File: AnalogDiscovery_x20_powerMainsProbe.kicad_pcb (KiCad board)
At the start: 2 copper layers, 64 x 64 mm, 32 parts, among them J1 Conn_02x15_Counter_Clockwise, J2 Conn_01x03_Female, J3 Conn_01x03_Female, J4 Conn_01x03_Male, J5 Conn_01x03_Male, J6 Conn_02x03_Counter_Clockwise

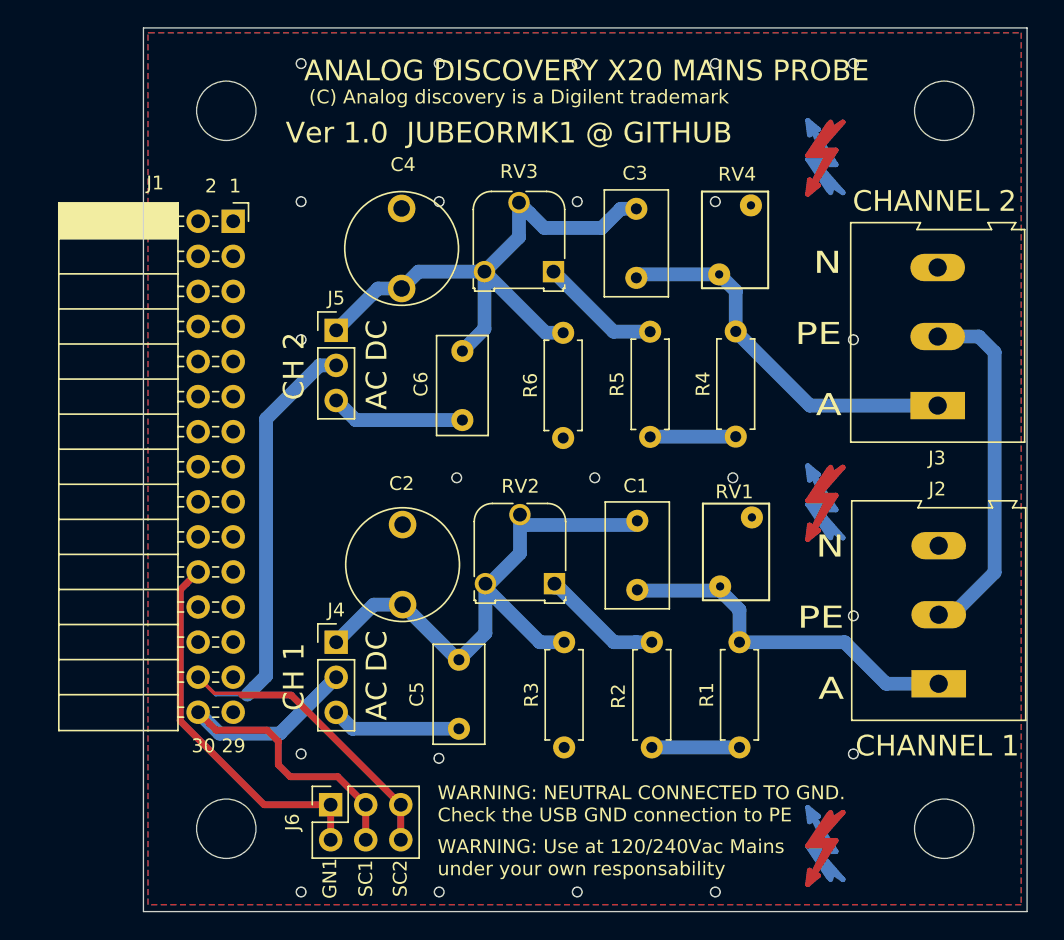
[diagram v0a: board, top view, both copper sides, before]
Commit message: Solved issue #10
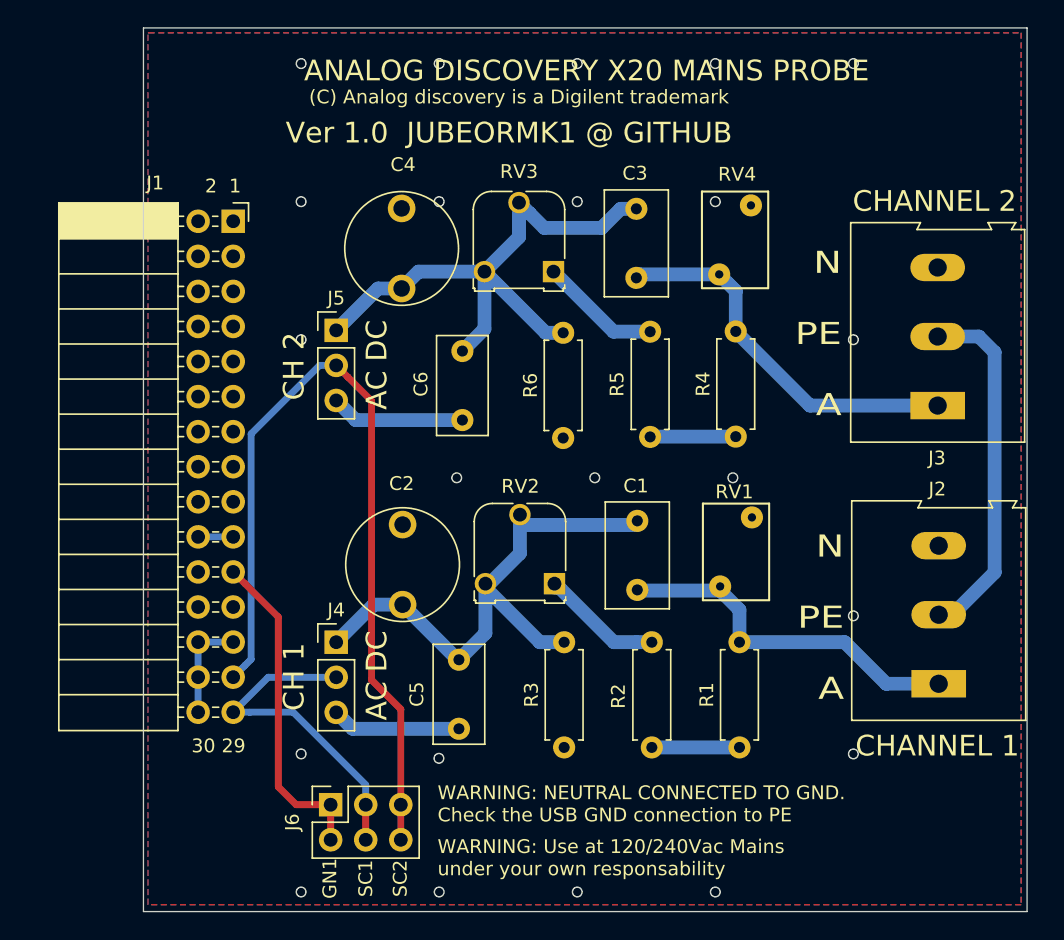
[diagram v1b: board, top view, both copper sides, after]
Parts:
- removed REF** (x6): Symbol_Highvoltage_Type1_CopperTop_Small, Symbol:Symbol_Highvoltage_Type1_CopperTop_Small
- removed REF** (x4): MountingHole_4.3mm_M4, MountingHole:MountingHole_4.3mm_M4
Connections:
- J1 pad 1: /DIO_15 -> (no net)
- J1 pad 10: /DIO_3 -> (no net)
- J1 pad 11: /DIO_10 -> (no net)
- J1 pad 12: /DIO_2 -> (no net)
- J1 pad 13: /DIO_9 -> (no net)
- J1 pad 14: /DIO_1 -> (no net)
- J1 pad 15: /DIO_8 -> (no net)
- J1 pad 16: /DIO_0 -> (no net)
- J1 pad 17: /TRIG_2 -> (no net)
- J1 pad 18: /TRIG_1 -> (no net)
- J1 pad 2: /DIO_7 -> (no net)
- J1 pad 21: /VOUT_AWG2 -> /VOUT_AWG1
- J1 pad 22: /VOUT_AWG1 -> (no net)
- J1 pad 23: /VOUT-5V0 -> (no net)
- J1 pad 24: /VOUT+5V0 -> (no net)
- J1 pad 27: GND -> /VIN_SC2_P
- J1 pad 28: /VIN_SC2_P -> GND
- J1 pad 29: GND -> /VIN_SC1_P
- J1 pad 3: /DIO_14 -> (no net)
- J1 pad 30: /VIN_SC1_P -> GND
- J1 pad 4: /DIO_6 -> (no net)
- J1 pad 5: /DIO_13 -> (no net)
- J1 pad 6: /DIO_5 -> (no net)
- J1 pad 7: /DIO_12 -> (no net)
- J1 pad 8: /DIO_4 -> (no net)
- J1 pad 9: /DIO_11 -> (no net)
- J2 pad 2: Net-(J2-Pad2) -> (no net)
- J3 pad 2: Net-(J3-Pad2) -> (no net)
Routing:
- net Earth_Protective: track 25.9 -> 0.00 mm
- net (no net): track 0.00 -> 25.9 mm
- net /VIN_SC2_P: track 52.4 -> 62.7 mm
- net GND: track 0.00 -> 10.2 mm
- net /VIN_SC1_P: track 30.8 -> 24.3 mm
- net /VOUT_AWG1: track 27.3 -> 23.8 mm

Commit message: Issue #3 fixed.
J1 aligned with board edge
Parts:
- moved J1 2.20 mm to (114.8, 80.0)
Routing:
- net /VOUT_AWG1: track 23.8 -> 26.0 mm
- net /VIN_SC2_P: track 62.7 -> 64.9 mm
- net /VIN_SC1_P: track 24.3 -> 26.5 mm
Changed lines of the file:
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@@
     (thickness 1.6)
     (drawings 25)
-    (tracks 107)
+    (tracks 111)
     (zones 0)
     (modules 22)
@@
     (35 F.Paste user hide)
     (36 B.SilkS user hide)
-    (37 F.SilkS user hide)
+    (37 F.SilkS user)
     (38 B.Mask user hide)
     (39 F.Mask user hide)
@@
     (uvia_dia 0.3048)
     (uvia_drill 0.15)
-    (add_net /DIO_0)
-    (add_net /DIO_1)
-    (add_net /DIO_10)
-    (add_net /DIO_11)
-    (add_net /DIO_12)
-    (add_net /DIO_13)
-    (add_net /DIO_14)
-    (add_net /DIO_15)
-    (add_net /DIO_2)
-    (add_net /DIO_3)
-    (add_net /DIO_4)
-    (add_net /DIO_5)
-    (add_net /DIO_6)
-    (add_net /DIO_7)
-    (add_net /DIO_8)
-    (add_net /DIO_9)
-    (add_net /TRIG_1)
-    (add_net /TRIG_2)
     (add_net /VIN_SC1_P)
     (add_net /VIN_SC2_P)
-    (add_net /VOUT+5V0)
-    (add_net /VOUT-5V0)
     (add_net /VOUT_AWG1)
-    (add_net /VOUT_AWG2)
     (add_net "Net-(C1-Pad1)")
     (add_net "Net-(C3-Pad1)")
     (add_net "Net-(C5-Pad2)")
     (add_net "Net-(C6-Pad2)")
-    (add_net "Net-(J2-Pad2)")
-    (add_net "Net-(J3-Pad2)")
   )
   (net_class "big clearance" ""
@@
   )
   (module Connector_PinSocket_2.54mm:PinSocket_2x15_P2.54mm_Horizontal (layer F.Cu)
-    (at 117 80)
+    (at 114.8 79.98)
     (descr "Through hole angled socket strip, 2x15, 2.54mm pitch, 8.51mm socket length, double cols (from Kicad 4.0.7), script generated")
     (tags "Through hole angled socket strip THT 2x15 2.54mm double row")
@@
   (gr_line (start 110.5 66) (end 174.5 66) (layer Edge.Cuts) (width 0.05))
   (gr_line (start 110.5 130) (end 110.5 66) (layer Edge.Cuts) (width 0.05))
+  (segment (start 169.09 108.5) (end 168.1 108.5) (width 1) (layer B.Cu) (net 0))
+  (segment (start 172.150001 105.439999) (end 169.09 108.5) (width 1) (layer B.Cu) (net 0))
+  (segment (start 172.150001 89.495001) (end 172.150001 105.439999) (width 1) (layer B.Cu) (net 0))
+  (segment (start 171.005 88.35) (end 172.150001 89.495001) (width 1) (layer B.Cu) (net 0))
+  (segment (start 168.025 88.35) (end 171.005 88.35) (width 1) (layer B.Cu) (net 0))
   (segment (start 126.6 124.8) (end 126.6 122.26) (width 0.5) (layer F.Cu) (net 1))
+  (segment (start 119.53 113.03) (end 117 115.56) (width 0.5) (layer B.Cu) (net 1))
+  (segment (start 124.46 113.03) (end 119.53 113.03) (width 0.5) (layer B.Cu) (net 1))
+  (segment (start 118.202081 115.56) (end 117 115.56) (width 0.5) (layer B.Cu) (net 1))
+  (segment (start 121.342002 115.56) (end 118.202081 115.56) (width 0.5) (layer B.Cu) (net 1))
+  (segment (start 126.6 120.817998) (end 121.342002 115.56) (width 0.5) (layer B.Cu) (net 1))
+  (segment (start 126.6 122.26) (end 126.6 120.817998) (width 0.5) (layer B.Cu) (net 1))
+  (segment (start 116.98 115.54) (end 114.8 115.54) (width 0.5) (layer B.Cu) (net 1))
+  (segment (start 117 115.56) (end 116.98 115.54) (width 0.5) (layer B.Cu) (net 1))
   (segment (start 129.14 122.26) (end 129.14 124.8) (width 0.5) (layer F.Cu) (net 2))
+  (segment (start 129.14 122.26) (end 129.14 115.34) (width 0.5) (layer F.Cu) (net 2))
+  (segment (start 125.309999 91.289999) (end 124.46 90.44) (width 0.5) (layer F.Cu) (net 2))
+  (segment (start 127.019999 92.999999) (end 125.309999 91.289999) (width 0.5) (layer F.Cu) (net 2))
+  (segment (start 127.019999 113.219999) (end 127.019999 92.999999) (width 0.5) (layer F.Cu) (net 2))
+  (segment (start 129.14 115.34) (end 127.019999 113.219999) (width 0.5) (layer F.Cu) (net 2))
+  (segment (start 116.98 113) (end 114.8 113) (width 0.5) (layer B.Cu) (net 2))
+  (segment (start 117 113.02) (end 116.98 113) (width 0.5) (layer B.Cu) (net 2))
+  (segment (start 118.300001 111.719999) (end 117 113.02) (width 0.5) (layer B.Cu) (net 2))
+  (segment (start 118.300001 95.397918) (end 118.300001 111.719999) (width 0.5) (layer B.Cu) (net 2))
+  (segment (start 124.46 90.44) (end 123.257919 90.44) (width 0.5) (layer B.Cu) (net 2))
+  (segment (start 123.257919 90.44) (end 118.300001 95.397918) (width 0.5) (layer B.Cu) (net 2))
   (segment (start 124.06 124.8) (end 124.06 122.26) (width 0.5) (layer F.Cu) (net 3))
+  (segment (start 116.98 105.38) (end 114.8 105.38) (width 0.5) (layer F.Cu) (net 3))
+  (segment (start 120.269999 108.669999) (end 116.98 105.38) (width 0.5) (layer F.Cu) (net 3))
+  (segment (start 120.269999 120.969999) (end 120.269999 108.669999) (width 0.5) (layer F.Cu) (net 3))
+  (segment (start 124.06 122.26) (end 121.56 122.26) (width 0.5) (layer F.Cu) (net 3))
+  (segment (start 121.56 122.26) (end 120.269999 120.969999) (width 0.5) (layer F.Cu) (net 3))
   (via (at 121.92 68.58) (size 0.8) (drill 0.6) (layers F.Cu B.Cu) (net 4))
   (via (at 131.92 68.58) (size 0.8) (drill 0.6) (layers F.Cu B.Cu) (net 4))
@@
   (via (at 141.92 128.58) (size 0.8) (drill 0.6) (layers F.Cu B.Cu) (net 4))
   (via (at 151.92 128.58) (size 0.8) (drill 0.6) (layers F.Cu B.Cu) (net 4))
-  (segment (start 169.09 108.5) (end 168.1 108.5) (width 1) (layer B.Cu) (net 0))
-  (segment (start 172.150001 105.439999) (end 169.09 108.5) (width 1) (layer B.Cu) (net 0))
-  (segment (start 172.150001 89.495001) (end 172.150001 105.439999) (width 1) (layer B.Cu) (net 0))
-  (segment (start 171.005 88.35) (end 172.150001 89.495001) (width 1) (layer B.Cu) (net 0))
-  (segment (start 168.025 88.35) (end 171.005 88.35) (width 1) (layer B.Cu) (net 0))
-  (segment (start 119.53 113.03) (end 117 115.56) (width 0.5) (layer B.Cu) (net 1))
-  (segment (start 124.46 113.03) (end 119.53 113.03) (width 0.5) (layer B.Cu) (net 1))
-  (segment (start 118.202081 115.56) (end 117 115.56) (width 0.5) (layer B.Cu) (net 1))
-  (segment (start 121.342002 115.56) (end 118.202081 115.56) (width 0.5) (layer B.Cu) (net 1))
-  (segment (start 126.6 120.817998) (end 121.342002 115.56) (width 0.5) (layer B.Cu) (net 1))
-  (segment (start 126.6 122.26) (end 126.6 120.817998) (width 0.5) (layer B.Cu) (net 1))
-  (segment (start 117.849999 112.170001) (end 117 113.02) (width 0.5) (layer B.Cu) (net 2))
-  (segment (start 118.300001 111.719999) (end 117.849999 112.170001) (width 0.5) (layer B.Cu) (net 2))
-  (segment (start 118.300001 95.397918) (end 118.300001 111.719999) (width 0.5) (layer B.Cu) (net 2))
-  (segment (start 123.257919 90.44) (end 118.300001 95.397918) (width 0.5) (layer B.Cu) (net 2))
-  (segment (start 124.46 90.44) (end 123.257919 90.44) (width 0.5) (layer B.Cu) (net 2))
-  (segment (start 129.14 122.26) (end 129.14 115.34) (width 0.5) (layer F.Cu) (net 2))
-  (segment (start 125.309999 91.289999) (end 124.46 90.44) (width 0.5) (layer F.Cu) (net 2))
-  (segment (start 127.019999 92.999999) (end 125.309999 91.289999) (width 0.5) (layer F.Cu) (net 2))
-  (segment (start 127.019999 113.219999) (end 127.019999 92.999999) (width 0.5) (layer F.Cu) (net 2))
-  (segment (start 129.14 115.34) (end 127.019999 113.219999) (width 0.5) (layer F.Cu) (net 2))
-  (segment (start 124.06 122.26) (end 121.56 122.26) (width 0.5) (layer F.Cu) (net 3))
-  (segment (start 117.849999 106.249999) (end 117 105.4) (width 0.5) (layer F.Cu) (net 3))
-  (segment (start 120.269999 108.669999) (end 117.849999 106.249999) (width 0.5) (layer F.Cu) (net 3))
-  (segment (start 120.269999 120.969999) (end 120.269999 108.669999) (width 0.5) (layer F.Cu) (net 3))
-  (segment (start 121.56 122.26) (end 120.269999 120.969999) (width 0.5) (layer F.Cu) (net 3))
-  (segment (start 114.46 115.56) (end 114.46 110.48) (width 0.5) (layer B.Cu) (net 4))
-  (segment (start 114.46 110.48) (end 117 110.48) (width 0.5) (layer B.Cu) (net 4))
-  (segment (start 117 102.86) (end 114.46 102.86) (width 0.5) (layer B.Cu) (net 4))
+  (segment (start 112.26 115.54) (end 112.26 113) (width 0.5) (layer B.Cu) (net 4))
+  (segment (start 112.26 113) (end 112.26 110.46) (width 0.5) (layer B.Cu) (net 4))
+  (segment (start 112.26 110.46) (end 114.8 110.46) (width 0.5) (layer B.Cu) (net 4))
+  (segment (start 112.26 102.84) (end 114.8 102.84) (width 0.5) (layer B.Cu) (net 4))
   (segment (start 161.29 110.49) (end 153.67 110.49) (width 1) (layer B.Cu) (net 5))
   (segment (start 168.1 113.5) (end 164.3 113.5) (width 1) (layer B.Cu) (net 5))

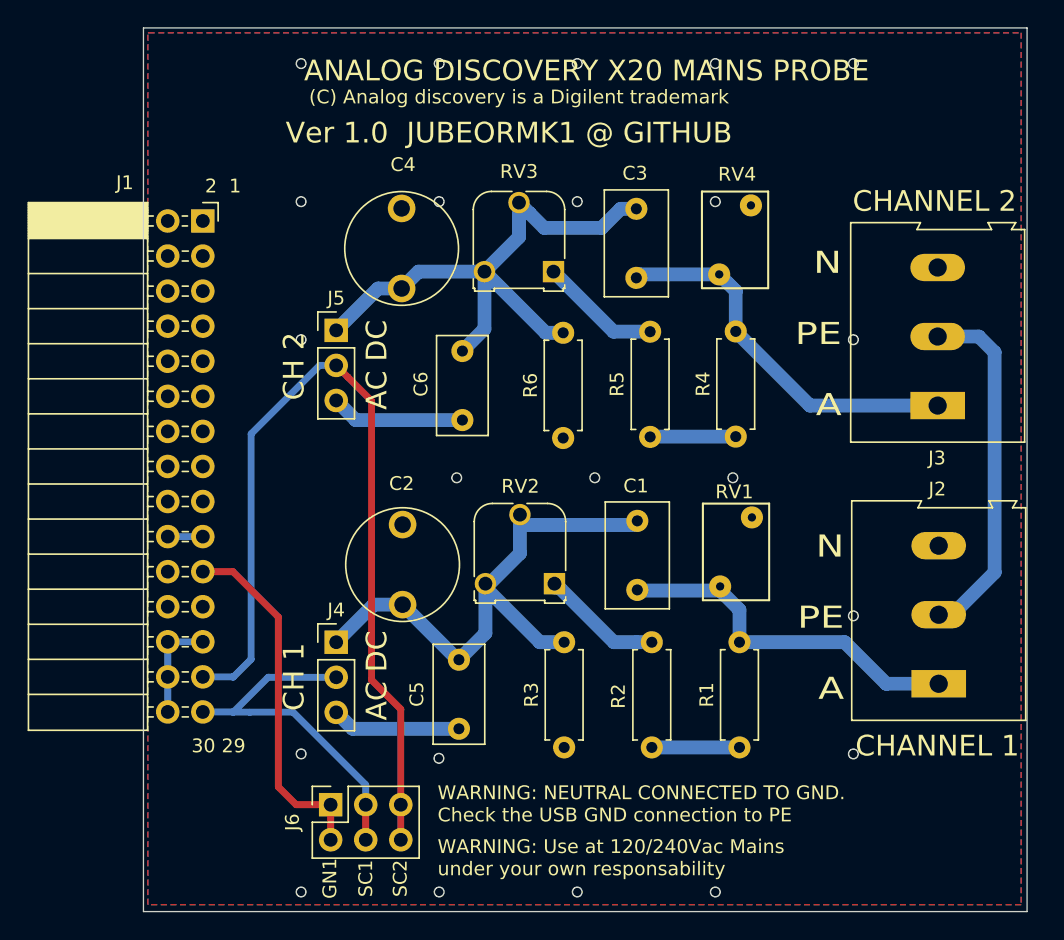
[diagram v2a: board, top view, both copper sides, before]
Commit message: Issue #9 fixed. The resistor pin separation has been change from 6 to 10mm
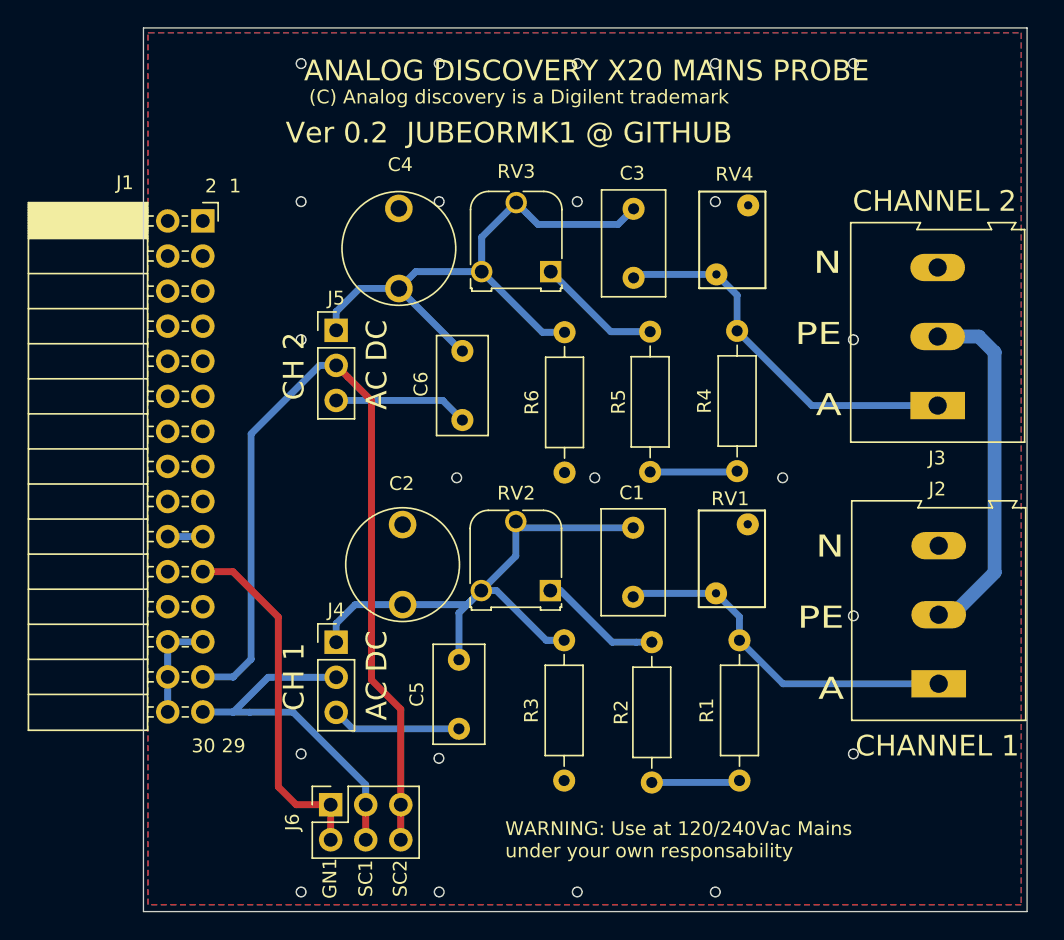
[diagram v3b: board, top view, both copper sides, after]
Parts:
- R1, R2, R3, R4, R5, R6: footprint Resistor_THT:R_Axial_DIN0207_L6.3mm_D2.5mm_P7.62mm_Horizontal -> Resistor_THT:R_Axial_DIN0207_L6.3mm_D2.5mm_P10.16mm_Horizontal
- moved R4 2.50 mm to (153.5, 98.1)
- moved R6 2.50 mm to (141.0, 98.2)
- moved R1 2.40 mm to (153.7, 120.5)
- moved R3 2.40 mm to (141.0, 120.5)
- moved C1 0.58 mm to (146.0, 102.2)
- moved RV1 0.58 mm to (152.0, 107.0)
- moved RV2 0.58 mm to (140.0, 106.8)
- moved C3 0.20 mm to (146.0, 79.1)
- moved C4 0.20 mm to (129.0, 82.0)
- moved RV3 0.20 mm to (140.0, 83.7)
- moved RV4 0.20 mm to (152.0, 83.8)
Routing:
- net Net-(C1-Pad1): track 39.7 -> 40.7 mm
- net Net-(C3-Pad1): track 42.3 -> 43.0 mm
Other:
- board text added: "Ver 0.2 JUBEORMK1 @ GITHUB"
- board text removed: "Ver 1.0 JUBEORMK1 @ GITHUB"
